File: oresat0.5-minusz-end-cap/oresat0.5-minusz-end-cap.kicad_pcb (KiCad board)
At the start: 2 copper layers, 105.6 x 105.6 mm, 46 parts, among them J2 U.FL-R-SMA, U2 MMC5883MA, U3 MMC5883MA

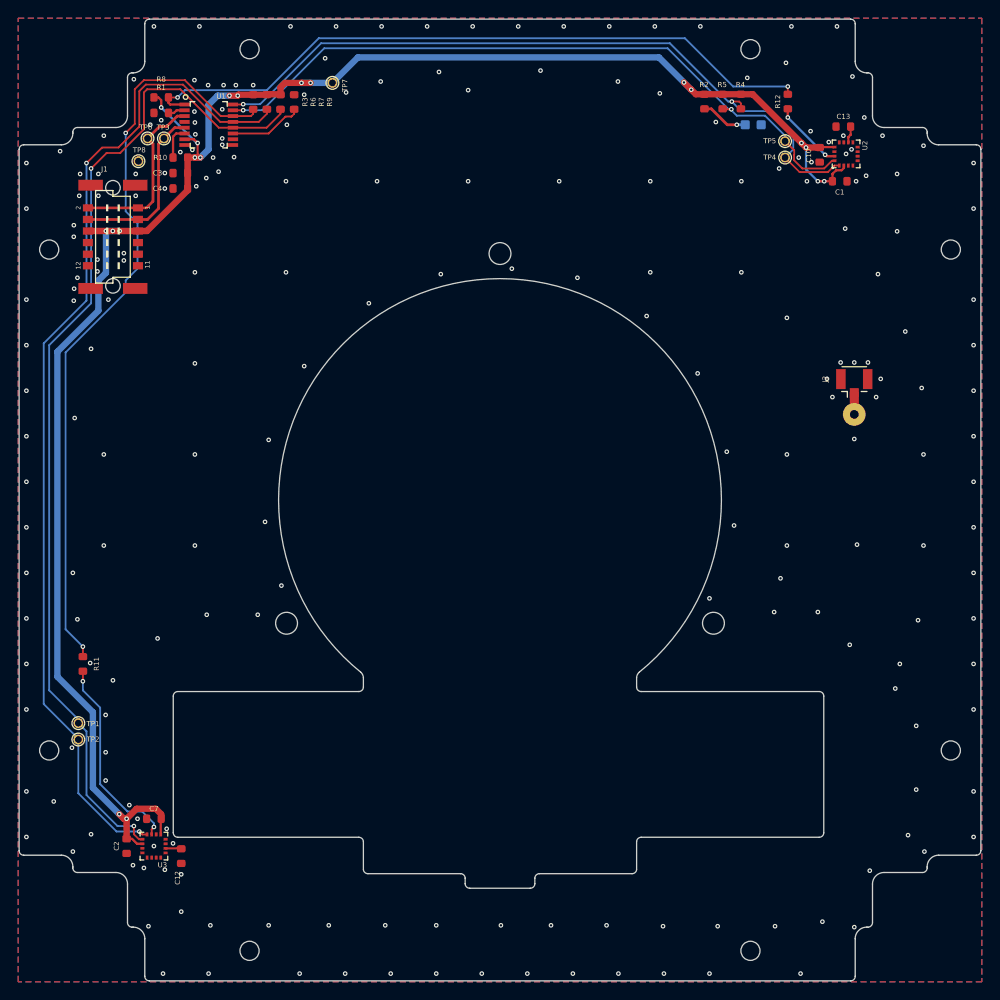
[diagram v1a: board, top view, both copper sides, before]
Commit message: Updated end caps
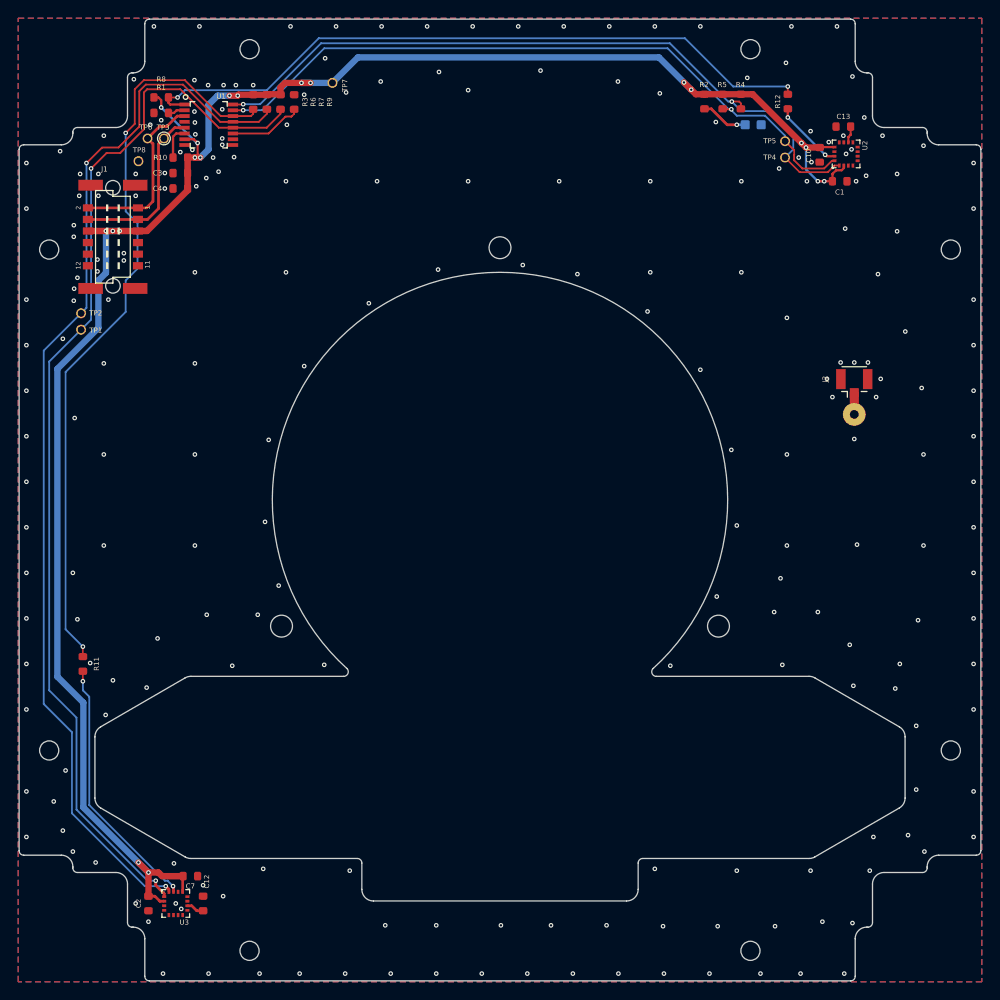
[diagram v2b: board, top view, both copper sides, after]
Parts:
- TP1, TP2, TP3, TP4, TP5, TP6, TP7, TP8: footprint oresat0.5-minusz-end-cap:1X01 -> oresat-misc:TestPoint-0.75mm-th
- moved TP2 46.8 mm to (102.5, 84.5)
- moved TP1 43.2 mm to (102.5, 86.3)
- moved C7 7.46 mm to (114.5, 146.3), turned to 0 degrees
- moved C2 6.74 mm to (109.9, 149.3)
- moved U3 6.74 mm to (112.9, 149.3)
- moved C12 5.73 mm to (115.9, 149.3), turned to 90 degrees
- moved REF** 0.64 mm to (124.5, 118.8)
- moved REF** 0.64 mm to (172.5, 118.8)
- moved REF** 0.64 mm to (148.5, 77.3)
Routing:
- net /SDA1: track 110.4 -> 117.2 mm
- net 3.3V: track 207.1 -> 213.7 mm
- net /SCL1: track 110.7 -> 117.3 mm
- net Net-(U3-INT): track 22.2 -> 28.5 mm
- net GND: vias 224 -> 232
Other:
- outline, holes or cut-outs redrawn
- board text added: "2023/08/02"
- board text added: "OreSat0.5 -Z End Cap v1.1"
- board text removed: "2022/02/19"
- board text removed: "OreSat0.5 -Z End Cap v1.0"

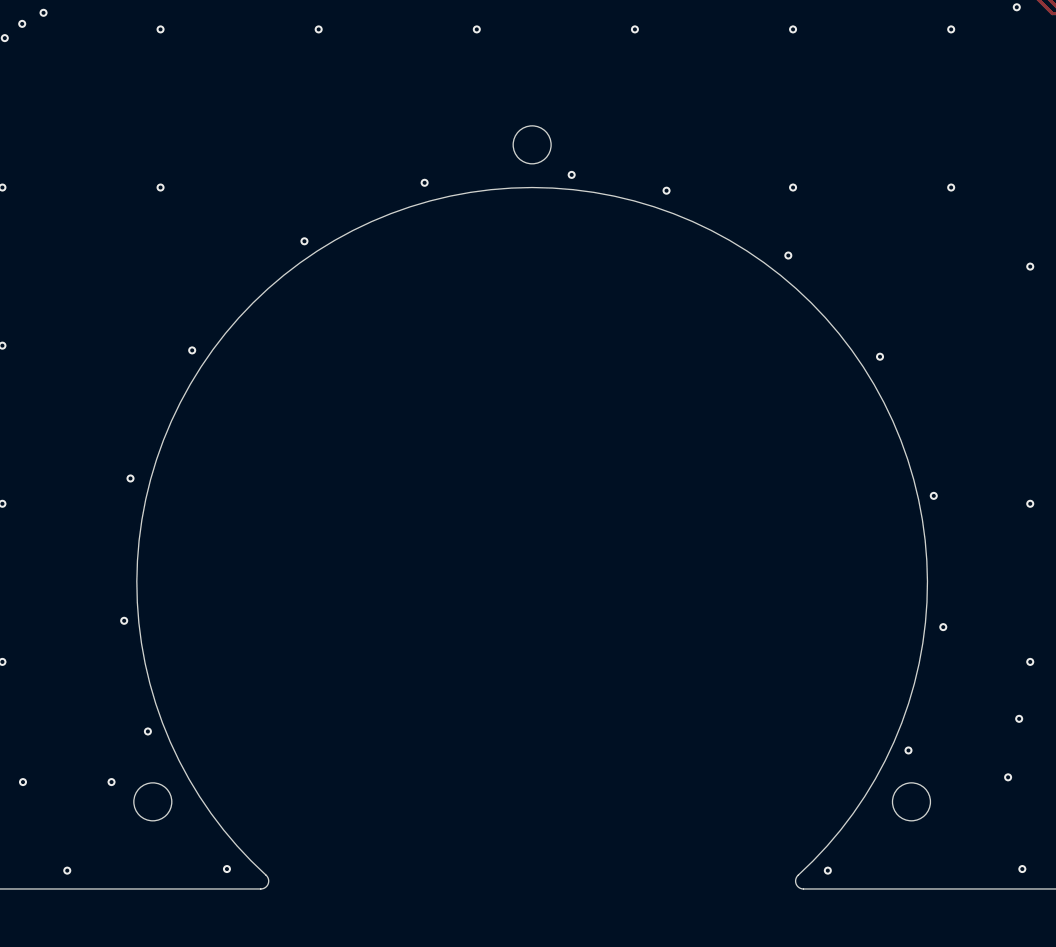
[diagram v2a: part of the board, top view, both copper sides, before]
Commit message: Updated mounting holes
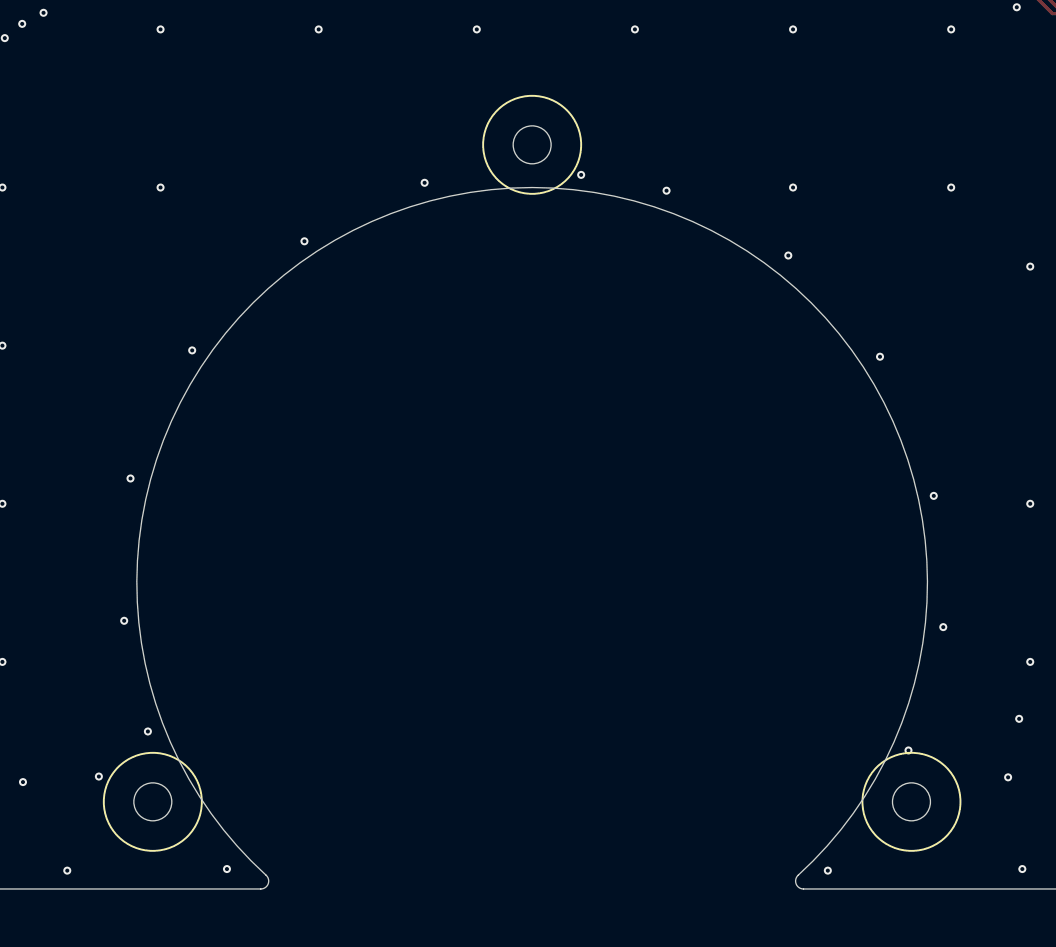
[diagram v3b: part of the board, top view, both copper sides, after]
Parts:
- REF** (x3): value Hole-2.4mm-NPTH -> M2-Mounting-Hole; footprint oresat-misc:Hole-2.4mm-NPTH -> oresat-misc:M2-Mounting-Hole
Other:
- board text added: "2023/09/10"
- board text removed: "2023/08/02"

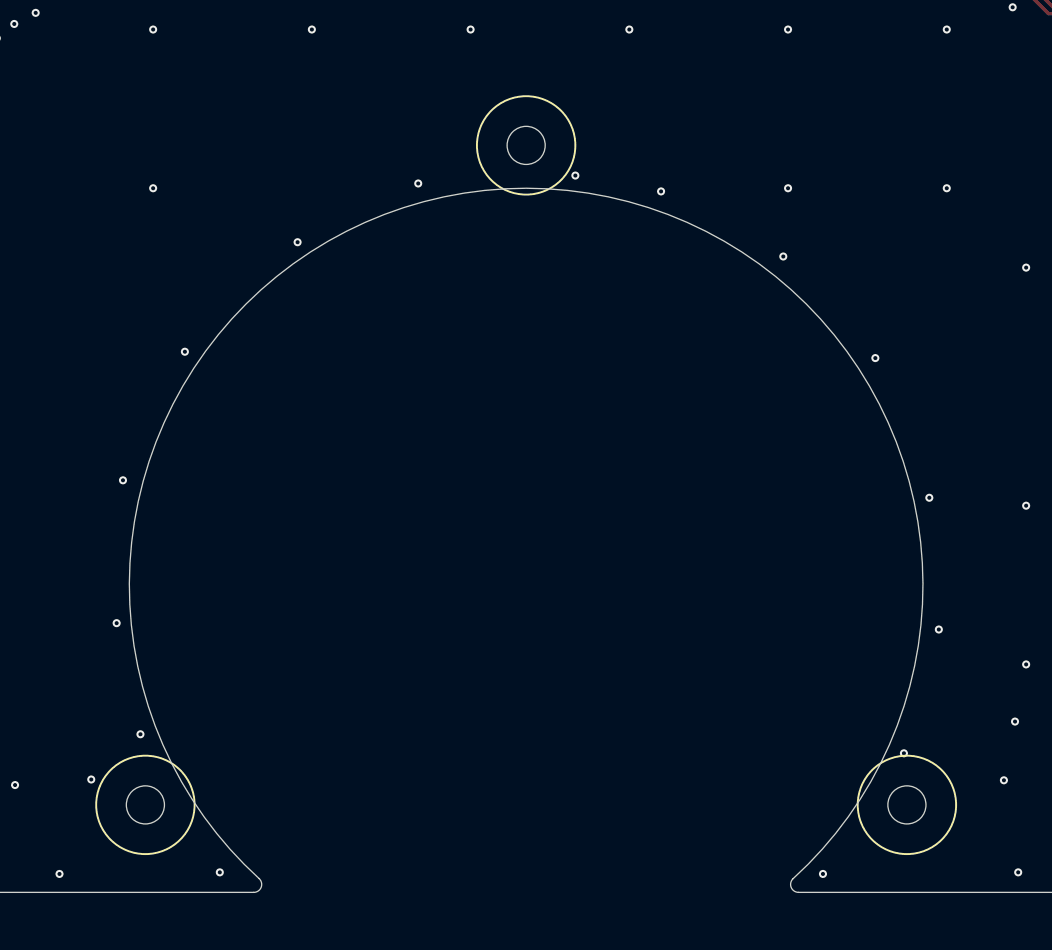
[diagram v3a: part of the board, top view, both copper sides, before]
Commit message: OreSat0.5 -Z end cap. Updated to latest KiCAD, fixed lack of holes for lens holder, and removed solder mask from around screw heads.
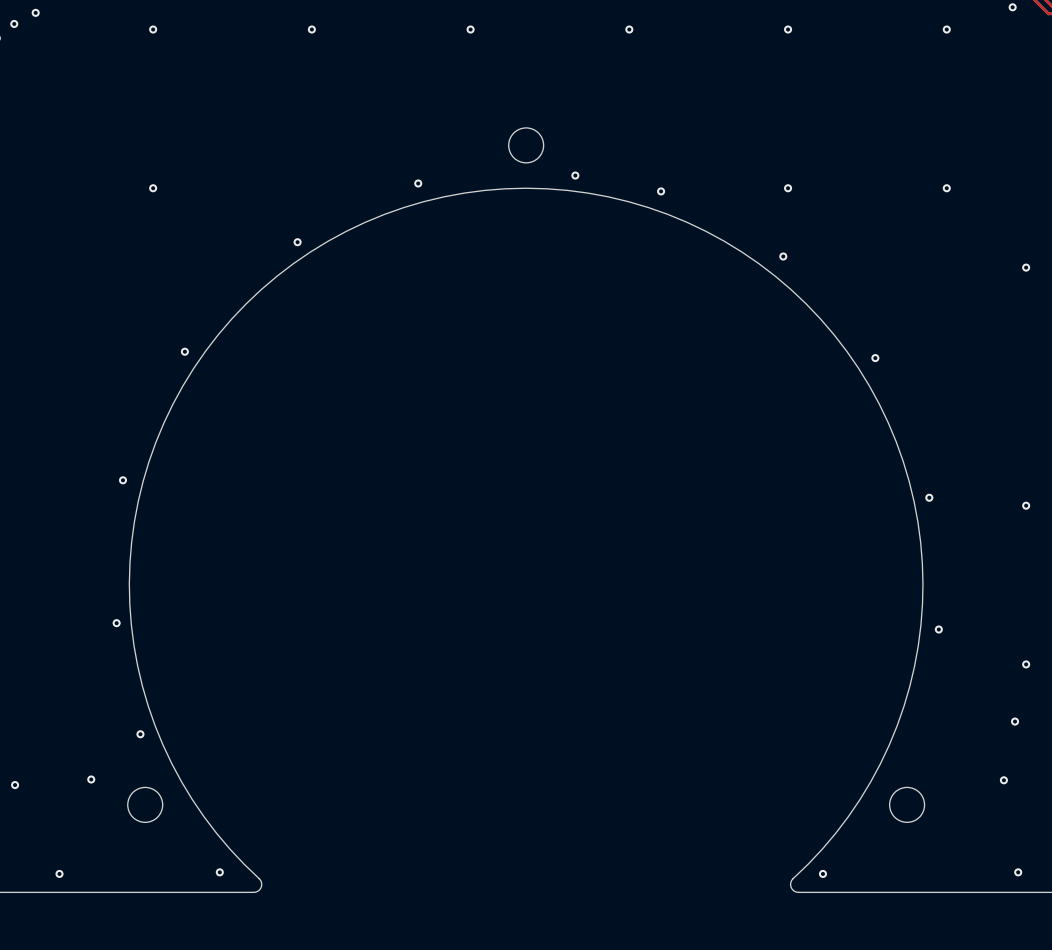
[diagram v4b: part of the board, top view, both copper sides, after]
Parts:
- removed the REF** at (124.5, 118.8)
- removed the REF** at (172.5, 118.8)
- removed the REF** at (148.5, 77.3)
- added REF**: MountingHole_2.1mm, MountingHole:MountingHole_2.1mm, B.Cu at (148.5, 77.3)
- added REF**: MountingHole_2.1mm, MountingHole:MountingHole_2.1mm, B.Cu at (124.5, 118.8)
- added REF**: MountingHole_2.1mm, MountingHole:MountingHole_2.1mm, B.Cu at (172.5, 118.8)
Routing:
- net GND: vias 232 -> 231

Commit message: updated mmc5883 magnetometer to mmc5983 for both OreSat 0.5 +Z and -Z endcaps
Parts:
- C1, C10, C12, C13, C2, C3, C4, C7, D2, J1, R1, R10, R2, R3, R4, R5, R6, R7, R8, R9: value (none) -> ~
- U1: value (none) -> LTC4305IGN
- U2, U3: value MMC5883MA -> MMC5983MA; footprint oresat0.5-minusz-end-cap:LGA-16(3X3) -> oresat-ics:LGA-16(3X3)
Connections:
- J1 pad 1: /MAG-SDA -> 3.3V
- J1 pad 2: /MAG-SDA -> 3.3V
- J1 pad 3: /MAG-SCL -> 3.3V
- J1 pad 4: /MAG-SCL -> 3.3V
- TP3 pad 1: /MAG-SCL -> 3.3V
- TP6 pad 1: /MAG-SDA -> 3.3V
- U2 pad 12: (no net) -> unconnected-(U2-NC-Pad12)
- U2 pad 14: (no net) -> unconnected-(U2-NC-Pad14)
- U2 pad 3: (no net) -> unconnected-(U2-NC-Pad3)
- U2 pad 4: (no net) -> 3.3V
- U2 pad 5: (no net) -> unconnected-(U2-SPI_SDO-Pad5)
- U2 pad 6: (no net) -> unconnected-(U2-NC-Pad6)
- U2 pad 7: (no net) -> unconnected-(U2-NC-Pad7)
- U2 pad 8: (no net) -> unconnected-(U2-NC-Pad8)
- U3 pad 12: (no net) -> unconnected-(U3-NC-Pad12)
- U3 pad 14: (no net) -> unconnected-(U3-NC-Pad14)
- U3 pad 3: (no net) -> unconnected-(U3-NC-Pad3)
- U3 pad 4: (no net) -> 3.3V
- U3 pad 5: (no net) -> unconnected-(U3-SPI_SDO-Pad5)
- U3 pad 6: (no net) -> unconnected-(U3-NC-Pad6)
- U3 pad 7: (no net) -> unconnected-(U3-NC-Pad7)
- U3 pad 8: (no net) -> unconnected-(U3-NC-Pad8)
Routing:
- net 3.3V: track 213.7 -> 217.1 mm
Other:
- board text added: "2024/03/04"
- board text added: "OreSat0.5 -Z End Cap v1.2"
- board text removed: "2023/09/10"
- board text removed: "OreSat0.5 -Z End Cap v1.1"

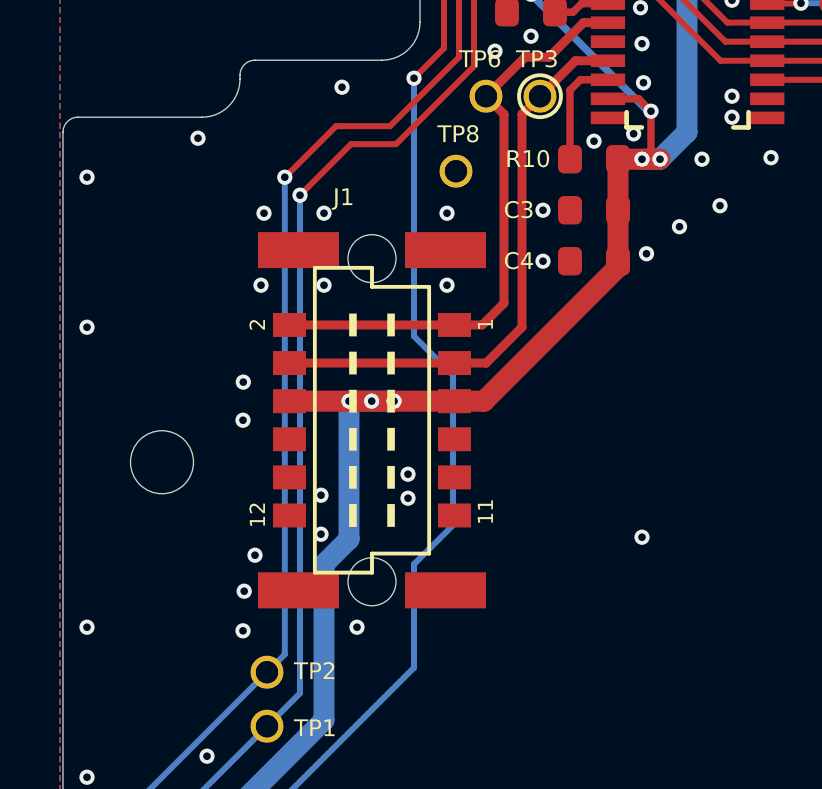
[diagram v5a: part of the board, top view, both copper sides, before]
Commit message: moved endcap harwin connectors on both +/-Z endcaps per move in Onshape
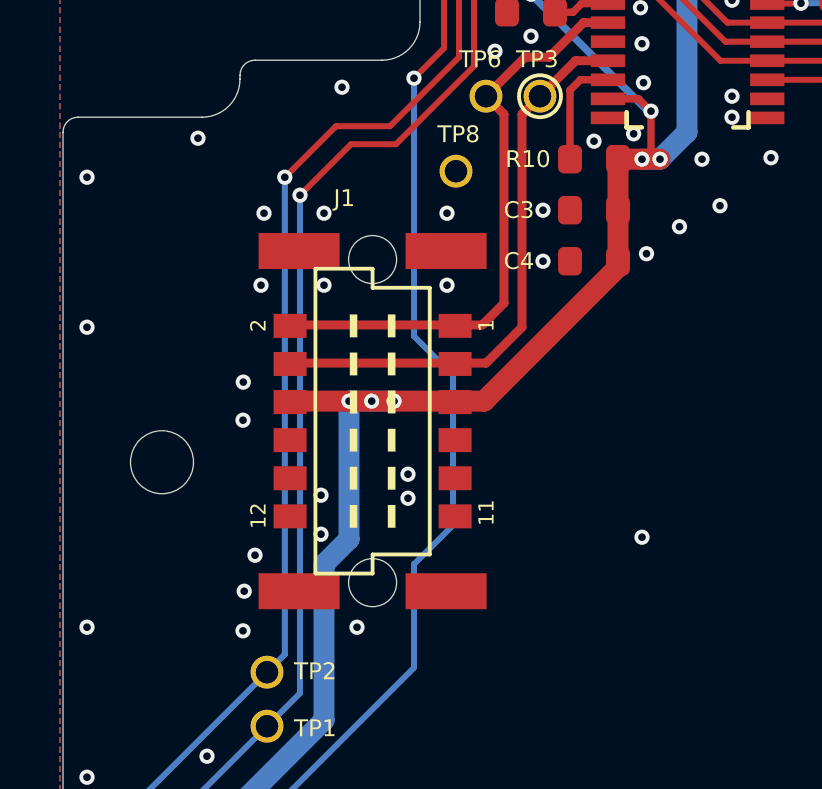
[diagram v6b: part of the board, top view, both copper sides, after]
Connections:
- J1 pad 1: 3.3V -> /MAG-SDA
- J1 pad 2: 3.3V -> /MAG-SDA
- J1 pad 3: 3.3V -> /MAG-SCL
- J1 pad 4: 3.3V -> /MAG-SCL
- TP3 pad 1: 3.3V -> /MAG-SCL
- TP6 pad 1: 3.3V -> /MAG-SDA
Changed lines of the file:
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@@
 			(layers "*.Cu" "*.Mask")
 			(remove_unused_layers no)
-			(net 1 "3.3V")
+			(net 26 "/MAG-SCL")
 			(pinfunction "1")
 			(pintype "passive")
@@
 	(footprint "oresat0.5-minusz-end-cap:HARWIN-M55-70X1242R"
 		(layer "F.Cu")
-		(at 106 76.1 90)
+		(at 106.02 76.13 90)
 		(property "Reference" "J1"
 			(at 7.1 -1.3 180)
@@
 			(size 0.8 1.1)
 			(layers "F.Cu" "F.Paste" "F.Mask")
-			(net 1 "3.3V")
+			(net 25 "/MAG-SDA")
 			(pinfunction "1")
 			(pintype "passive")
@@
 			(size 0.8 1.1)
 			(layers "F.Cu" "F.Paste" "F.Mask")
-			(net 1 "3.3V")
+			(net 25 "/MAG-SDA")
 			(pinfunction "2")
 			(pintype "passive")
@@
 			(size 0.8 1.1)
 			(layers "F.Cu" "F.Paste" "F.Mask")
-			(net 1 "3.3V")
+			(net 26 "/MAG-SCL")
 			(pinfunction "3")
 			(pintype "passive")
@@
 			(size 0.8 1.1)
 			(layers "F.Cu" "F.Paste" "F.Mask")
-			(net 1 "3.3V")
+			(net 26 "/MAG-SCL")
 			(pinfunction "4")
 			(pintype "passive")
@@
 			(layers "*.Cu" "*.Mask")
 			(remove_unused_layers no)
-			(net 1 "3.3V")
+			(net 25 "/MAG-SDA")
 			(pinfunction "1")
 			(pintype "passive")
@@
 	)
 	(gr_line
-		(start 108.1 81.285)
-		(end 103.9 70.915)
+		(start 108.12 81.315)
+		(end 103.92 70.945)
 		(stroke
 			(width 0.002)
@@
 	)
 	(gr_circle
-		(center 106 76.1)
-		(end 105.5 76.1)
+		(center 106.02 76.13)
+		(end 105.52 76.13)
 		(stroke
 			(width 0.002)
@@
 	)
 	(gr_circle
-		(center 106 76.1)
-		(end 105.5 76.1)
+		(center 106.02 76.13)
+		(end 105.52 76.13)
 		(stroke
 			(width 0.002)
@@
 	)
 	(gr_line
-		(start 108.1 70.915)
-		(end 103.9 81.285)
+		(start 108.12 70.945)
+		(end 103.92 81.315)
 		(stroke
 			(width 0.002)
